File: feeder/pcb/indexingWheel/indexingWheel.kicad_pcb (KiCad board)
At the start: 2 copper layers, 43 x 43 mm, 0 parts

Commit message: Adding the git hash to the feeder mobo, feeder floor and indexing wheel boards.
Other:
- board text added: "INDEXING WHEEL REV02 <<hash>>"
- board text removed: "INDEXING WHEEL REV02"
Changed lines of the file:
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@@
     (uvia_drill 0.1)
   )
-  (gr_text "INDEXING WHEEL\nREV02" (at 0 6.8) (layer F.Mask)
+  (gr_text "INDEXING WHEEL\nREV02\n<<hash>>" (at 0 6.8) (layer F.Mask)
     (effects (font (size 1.5 1.5) (thickness 0.3)))
   )

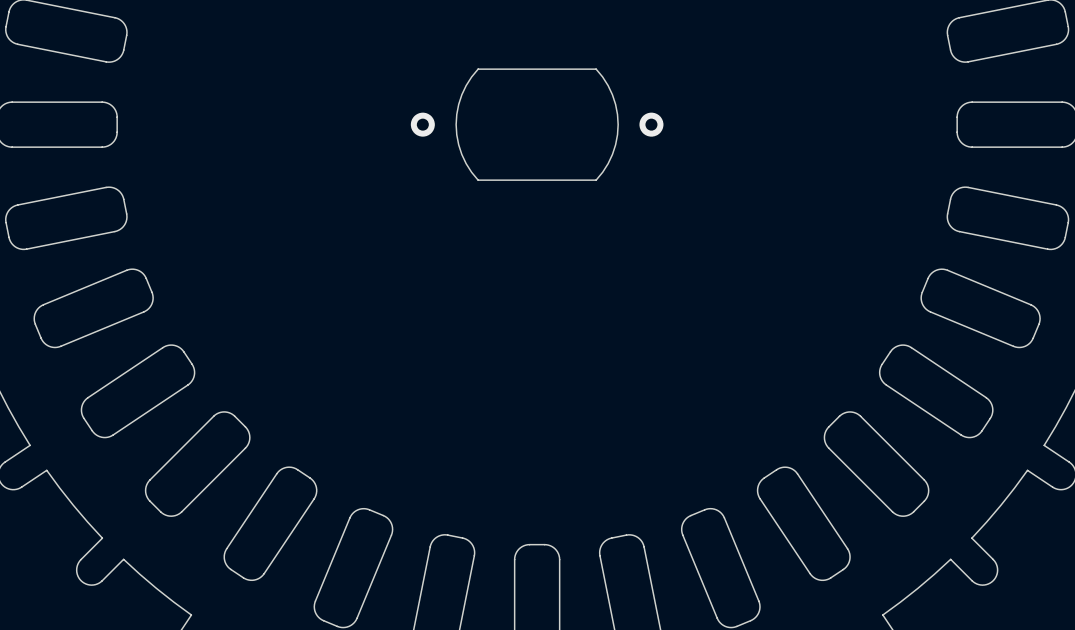
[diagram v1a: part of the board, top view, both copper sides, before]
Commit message: Add decorations to feeders
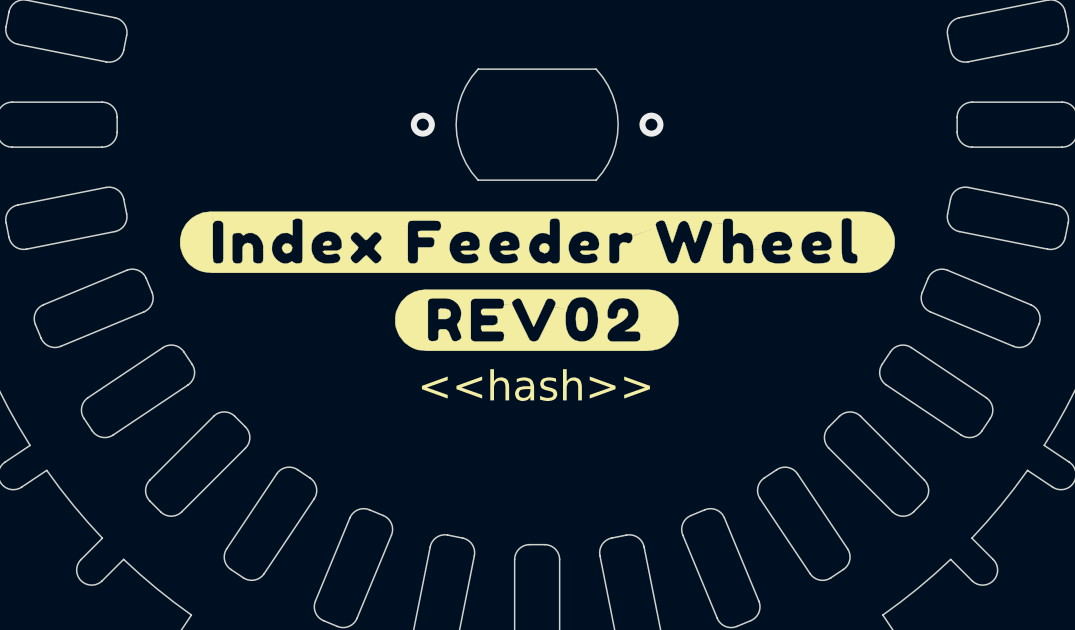
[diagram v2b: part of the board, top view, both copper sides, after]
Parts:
- added ?: , buzzard_labels, B.Cu at (-0.02, 3.89)
- added ?: , buzzard_labels, F.Cu at (0.01, 3.92)
- added ?: , buzzard_labels, B.Cu at (-0.11, 6.49)
- added ?: , buzzard_labels, F.Cu at (-0.01, 6.52)
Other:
- board text added: "<<hash>>"
- board text removed: "INDEXING WHEEL REV02 <<hash>>"
